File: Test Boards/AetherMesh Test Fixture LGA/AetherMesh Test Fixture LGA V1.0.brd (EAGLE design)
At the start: 71.2 x 57.5 mm, 5 parts, among them J1 POWER_JACKEJ508A, M1 AETHERMESH_MODULESMD_HOLES

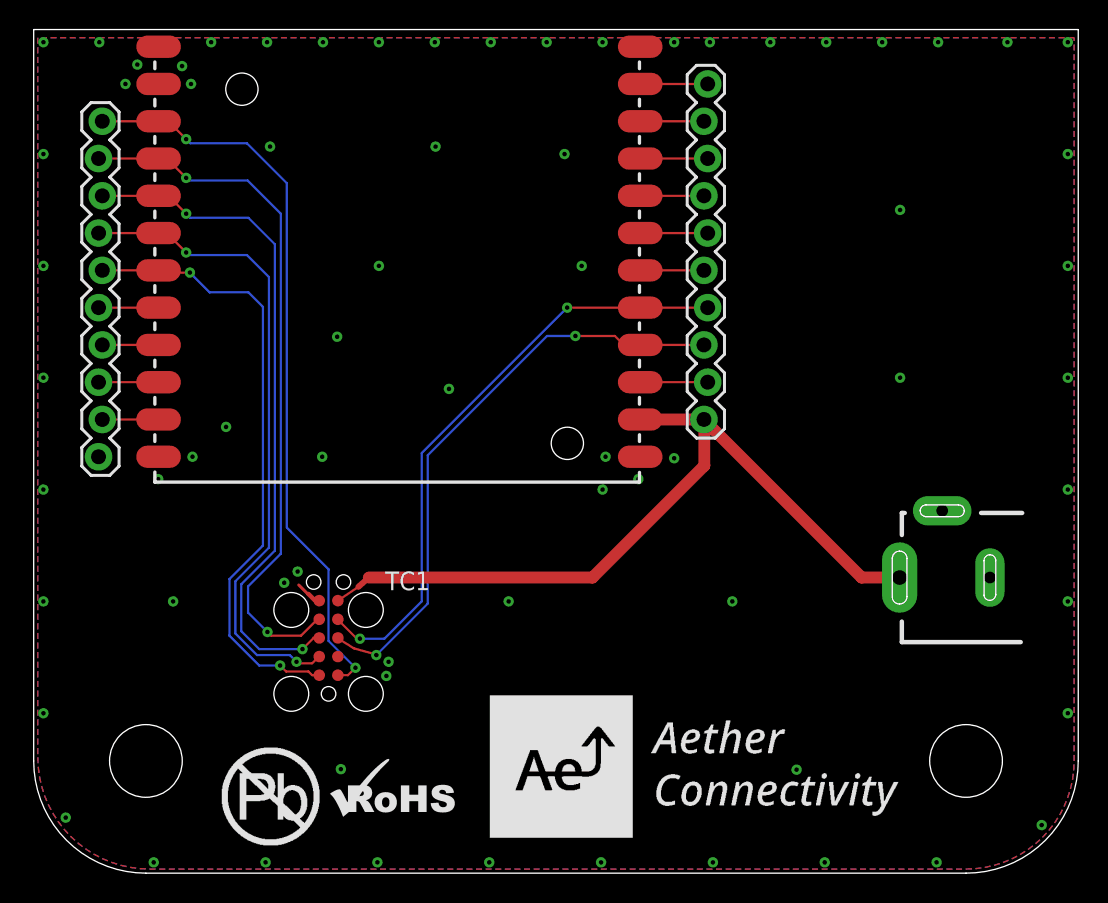
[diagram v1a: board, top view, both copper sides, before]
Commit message: Updated test boards with silkscreen pin names and current measurment jumper
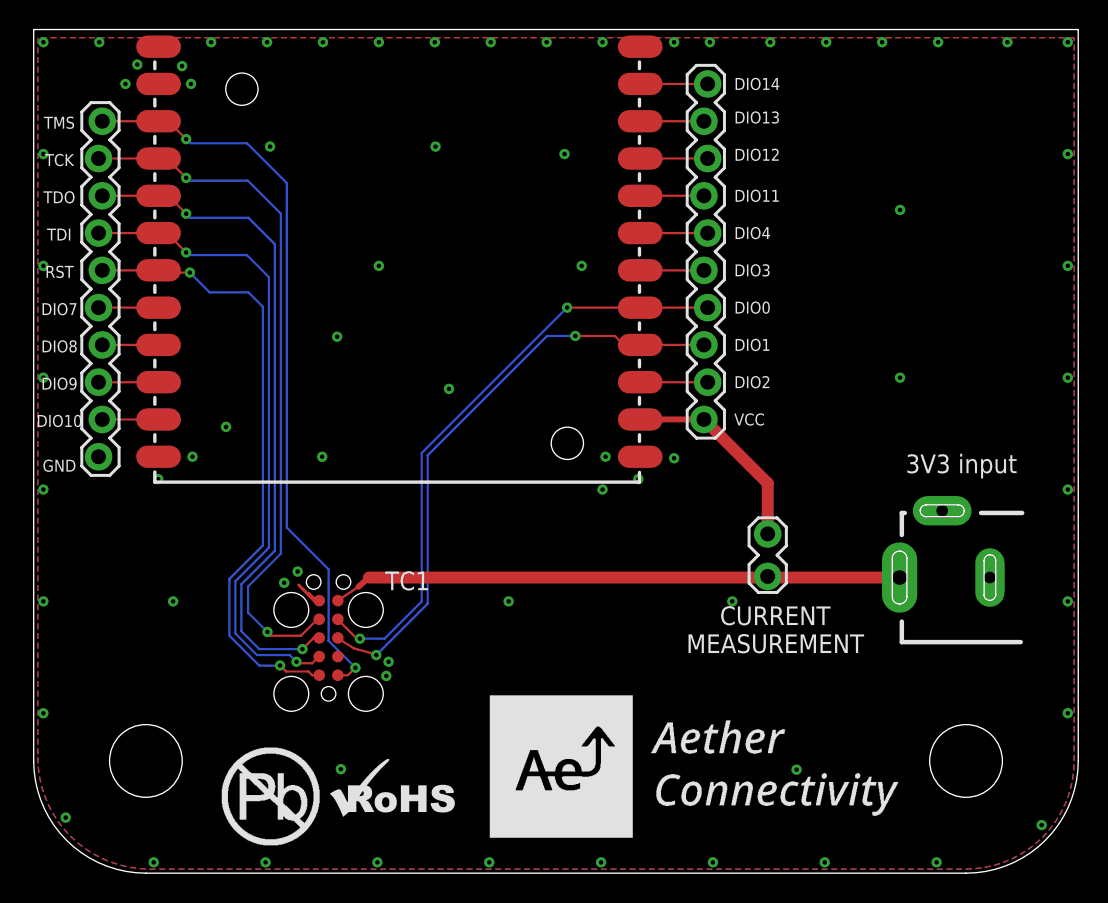
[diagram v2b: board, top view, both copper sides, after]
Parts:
- added JP3: (no value), 1. growflux:1X02_LOCK
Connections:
- new net N$3: JP2.10, JP3.1, M1.P$23
- net VCC: now also JP3.2; no longer JP2.10, M1.P$23
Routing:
- net VCC: track 53.9 -> 38.9 mm
- net N$3: track 0.00 -> 13.9 mm
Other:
- board text added: "3V3 input"
- board text added: "CURRENT MEASUREMENT"
- board text added: "DIO0"
- board text added: "DIO1"
- board text added: "DIO10"
- board text added: "DIO11"
- board text added: "DIO12"
- board text added: "DIO13"
- board text added: "DIO14"
- board text added: "DIO2"
- board text added: "DIO3"
- board text added: "DIO4"
- board text added: "DIO7"
- board text added: "DIO8"
- board text added: "DIO9"
- board text added: "GND"
- board text added: "RST"
- board text added: "TCK"
- board text added: "TDI"
- board text added: "TDO"
- board text added: "TMS"
- board text added: "VCC"
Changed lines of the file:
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@@
 <?xml version="1.0" encoding="utf-8"?>
 <!DOCTYPE eagle SYSTEM "eagle.dtd">
-<eagle version="8.3.2">
+<eagle version="8.4.1">
 <drawing>
 <settings>
@@
 <setting verticaltext="up"/>
 </settings>
-<grid distance="1" unitdist="inch" unit="inch" style="lines" multiple="1" display="yes" altdistance="0.025" altunitdist="inch" altunit="inch"/>
+<grid distance="0.01" unitdist="inch" unit="inch" style="lines" multiple="1" display="yes" altdistance="0.025" altunitdist="inch" altunit="inch"/>
 <layers>
 <layer number="1" name="Top" color="4" fill="1" visible="yes" active="yes"/>
@@
 <rectangle x1="30.8483" y1="11.717021875" x2="40.5917375" y2="11.752578125" layer="21"/>
 <rectangle x1="30.8483" y1="11.75258125" x2="40.5917375" y2="11.7881375" layer="21"/>
+<text x="59.182" y="26.924" size="1.27" layer="21" font="vector">3V3 input</text>
+<text x="50.292" y="16.256" size="1.27" layer="21" font="vector" align="center">CURRENT
+MEASUREMENT</text>
+<text x="1.524" y="50.8" size="0.8128" layer="21" font="vector" ratio="12" align="center">TMS</text>
+<text x="1.524" y="48.26" size="0.8128" layer="21" font="vector" ratio="12" align="center">TCK</text>
+<text x="1.524" y="45.72" size="0.8128" layer="21" font="vector" ratio="12" align="center">TDO</text>
+<text x="1.524" y="43.18" size="0.8128" layer="21" font="vector" ratio="12" align="center">TDI</text>
+<text x="1.524" y="40.64" size="0.8128" layer="21" font="vector" ratio="12" align="center">RST</text>
+<text x="1.524" y="38.1" size="0.8128" layer="21" font="vector" ratio="12" align="center">DIO7</text>
+<text x="1.524" y="35.56" size="0.8128" layer="21" font="vector" ratio="12" align="center">DIO8</text>
+<text x="1.524" y="33.02" size="0.8128" layer="21" font="vector" ratio="12" align="center">DIO9</text>
+<text x="1.524" y="30.48" size="0.8128" layer="21" font="vector" ratio="12" align="center">DIO10</text>
+<text x="1.524" y="27.432" size="0.8128" layer="21" font="vector" ratio="12" align="center">GND
+</text>
+<text x="47.498" y="53.848" size="0.8128" layer="21" font="vector" ratio="12" align="top-left">DIO14</text>
+<text x="47.498" y="51.562" size="0.8128" layer="21" font="vector" ratio="12" align="top-left">DIO13</text>
+<text x="47.498" y="49.022" size="0.8128" layer="21" font="vector" ratio="12" align="top-left">DIO12</text>
+<text x="47.498" y="46.228" size="0.8128" layer="21" font="vector" ratio="12" align="top-left">DIO11</text>
+<text x="47.498" y="43.688" size="0.8128" layer="21" font="vector" ratio="12" align="top-left">DIO4</text>
+<text x="47.498" y="41.148" size="0.8128" layer="21" font="vector" ratio="12" align="top-left">DIO3</text>
+<text x="47.498" y="38.608" size="0.8128" layer="21" font="vector" ratio="12" align="top-left">DIO0</text>
+<text x="47.498" y="36.068" size="0.8128" layer="21" font="vector" ratio="12" align="top-left">DIO1</text>
+<text x="47.498" y="33.528" size="0.8128" layer="21" font="vector" ratio="12" align="top-left">DIO2</text>
+<text x="47.498" y="30.988" size="0.8128" layer="21" font="vector" ratio="12" align="top-left">VCC</text>
 </plain>
 <attributes>
@@
 <param name="dpMaxLengthDifference" value="10mm"/>
 <param name="dpGapFactor" value="2.5"/>
-<param name="checkGrid" value="0"/>
 <param name="checkAngle" value="0"/>
 <param name="checkFont" value="1"/>
 <param name="checkRestrict" value="1"/>
+<param name="checkStop" value="0"/>
 <param name="useDiameter" value="13"/>
 <param name="maxErrors" value="50"/>
@@
 <element name="JP1" library="3. growflux" package="1X10_LOCK" value="M10LOCK" x="4.318" y="28.0416" smashed="yes" rot="R90"/>
 <element name="JP2" library="3. growflux" package="1X10_LOCK" value="M10LOCK" x="45.5676" y="53.4416" smashed="yes" rot="R270"/>
+<element name="JP3" library="1. growflux" package="1X02_LOCK" value="" x="49.784" y="22.606" smashed="yes" rot="R270">
+<attribute name="VALUE" x="46.609" y="23.876" size="1.27" layer="27" rot="R270"/>
+</element>
 </elements>
 <signals>
@@
 </signal>
 <signal name="VCC">
-<contactref element="M1" pad="P$23"/>
 <contactref element="TC1" pad="9"/>
 <contactref element="J1" pad="3"/>
-<wire x1="58.7724" y1="19.812" x2="56.1848" y2="19.812" width="0.8128" layer="1"/>
-<wire x1="45.466" y1="30.5308" x2="56.1848" y2="19.812" width="0.8128" layer="1"/>
-<wire x1="45.4152" y1="30.5816" x2="41.0972" y2="30.5816" width="0.8128" layer="1"/>
 <wire x1="20.4978" y1="18.2372" x2="21.8948" y2="19.177" width="0.1524" layer="1"/>
-<contactref element="JP2" pad="10"/>
 <wire x1="21.8948" y1="19.177" x2="22.606" y2="19.812" width="0.4064" layer="1"/>
-<wire x1="22.606" y1="19.812" x2="37.846" y2="19.812" width="0.8128" layer="1"/>
-<wire x1="37.846" y1="19.812" x2="45.466" y2="27.432" width="0.8128" layer="1"/>
-<wire x1="45.466" y1="27.432" x2="45.466" y2="30.5308" width="0.8128" layer="1"/>
-<wire x1="45.466" y1="30.5308" x2="45.4152" y2="30.5816" width="0.8128" layer="1"/>
-<wire x1="45.4152" y1="30.5816" x2="45.4406" y2="30.5816" width="0" layer="19" extent="1-1"/>
+<contactref element="JP3" pad="2"/>
+<wire x1="49.7078" y1="19.812" x2="49.784" y2="19.8882" width="0.8128" layer="1"/>
+<wire x1="22.606" y1="19.812" x2="49.7078" y2="19.812" width="0.8128" layer="1"/>
+<wire x1="58.7724" y1="19.812" x2="49.7078" y2="19.812" width="0.8128" layer="1"/>
 </signal>
 <signal name="N$2">
@@
 <wire x1="41.0972" y1="53.4416" x2="45.6946" y2="53.4416" width="0.1524" layer="1"/>
 </signal>
+<signal name="N$3">
+<contactref element="M1" pad="P$23"/>
+<contactref element="JP2" pad="10"/>
+<contactref element="JP3" pad="1"/>
+<wire x1="45.4406" y1="30.5816" x2="49.784" y2="26.2382" width="0.8128" layer="1"/>
+<wire x1="49.784" y1="26.2382" x2="49.784" y2="22.7838" width="0.8128" layer="1"/>
+<wire x1="41.0972" y1="30.5816" x2="45.4406" y2="30.5816" width="0.4064" layer="1"/>
+</signal>
 </signals>

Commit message: Updated reference designs and test boards with latest XDS programmer tag connect header
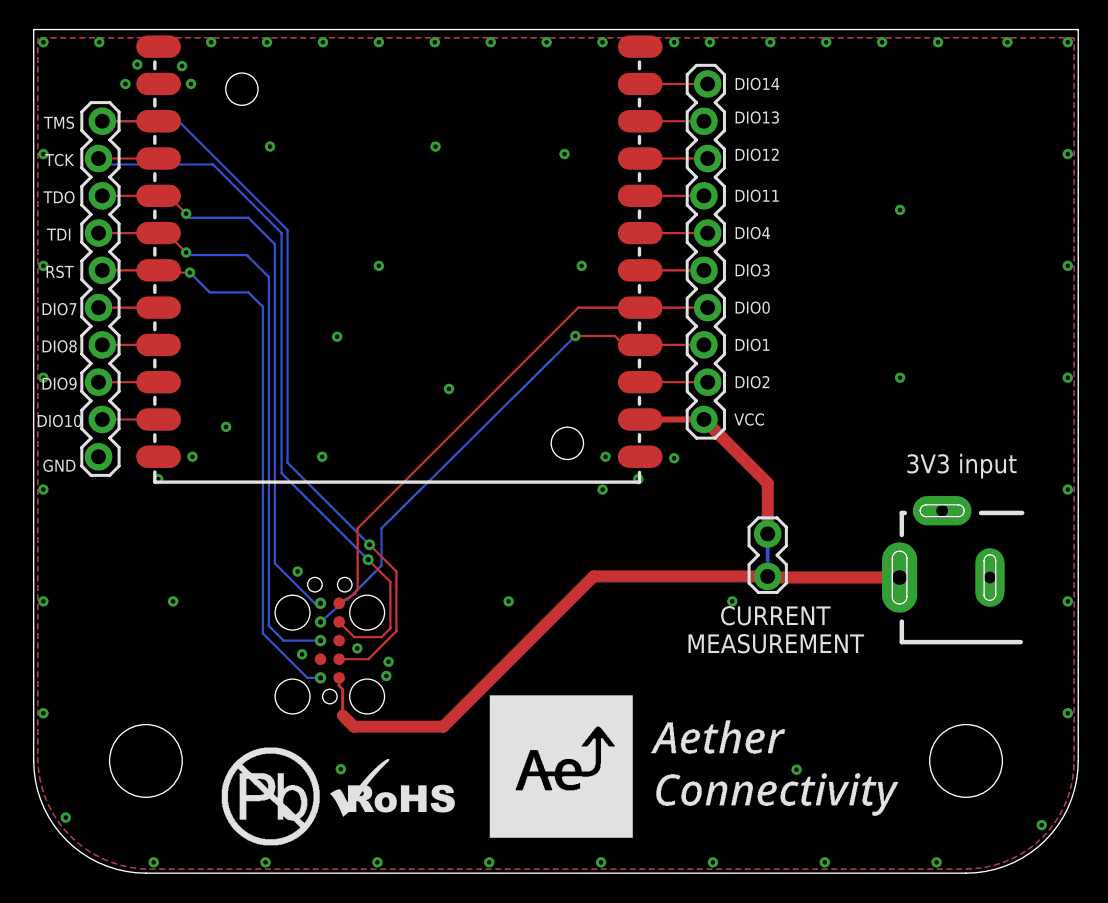
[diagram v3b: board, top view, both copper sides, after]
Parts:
- removed TC1: TC2050-IDC, TagConnect:TC2050-IDC
- added TC3: TC2050-IDC, TagConnect:TC2050-IDC
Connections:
- net DIO0-RX: now also TC3.5; no longer TC1.7
- net DIO1-TX: now also TC3.7; no longer TC1.5
- net GND: now also TC3.3, TC3.9; no longer TC1.10, TC1.3
- net RESET: now also TC3.10; no longer TC1.2
- net TCK: now also TC3.4; no longer TC1.8
- net TDI: now also TC3.8; no longer TC1.4
- net TDO: now also TC3.6; no longer TC1.6
- net TMS: now also TC3.2; no longer TC1.1
- net VCC: now also TC3.1; no longer TC1.9
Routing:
- net VCC: track 38.9 -> 48.1 mm
- net TDO: track 46.6 -> 39.1 mm
- net TCK: track 48.0 -> 53.4 mm, vias 2 -> 1
- net DIO0-RX: track 41.0 -> 35.8 mm, vias 2 -> 0
- net TMS: track 50.7 -> 55.3 mm, vias 2 -> 1
- net DIO1-TX: track 40.4 -> 35.9 mm
- net TDI: track 44.8 -> 40.6 mm
- net RESET: track 42.7 -> 39.5 mm
- net GND: track 1.84 -> 0.00 mm, vias 70 -> 71
